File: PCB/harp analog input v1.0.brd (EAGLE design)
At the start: 86.8 x 80 mm, 112 parts, among them IC1 USBLC6-2SC6, IC10 SN74LVC1G125, IC11 SN74LVC1G125, IC12 SN74LVC1G125, IC13 AD7606-4, IC14 M74VHC1GT50DTT1G, IC15 M74VHC1GT50DTT1G, IC2 DC-DC-SIP-5, IC3 FT232RL, IC4 TPS78630DCQ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

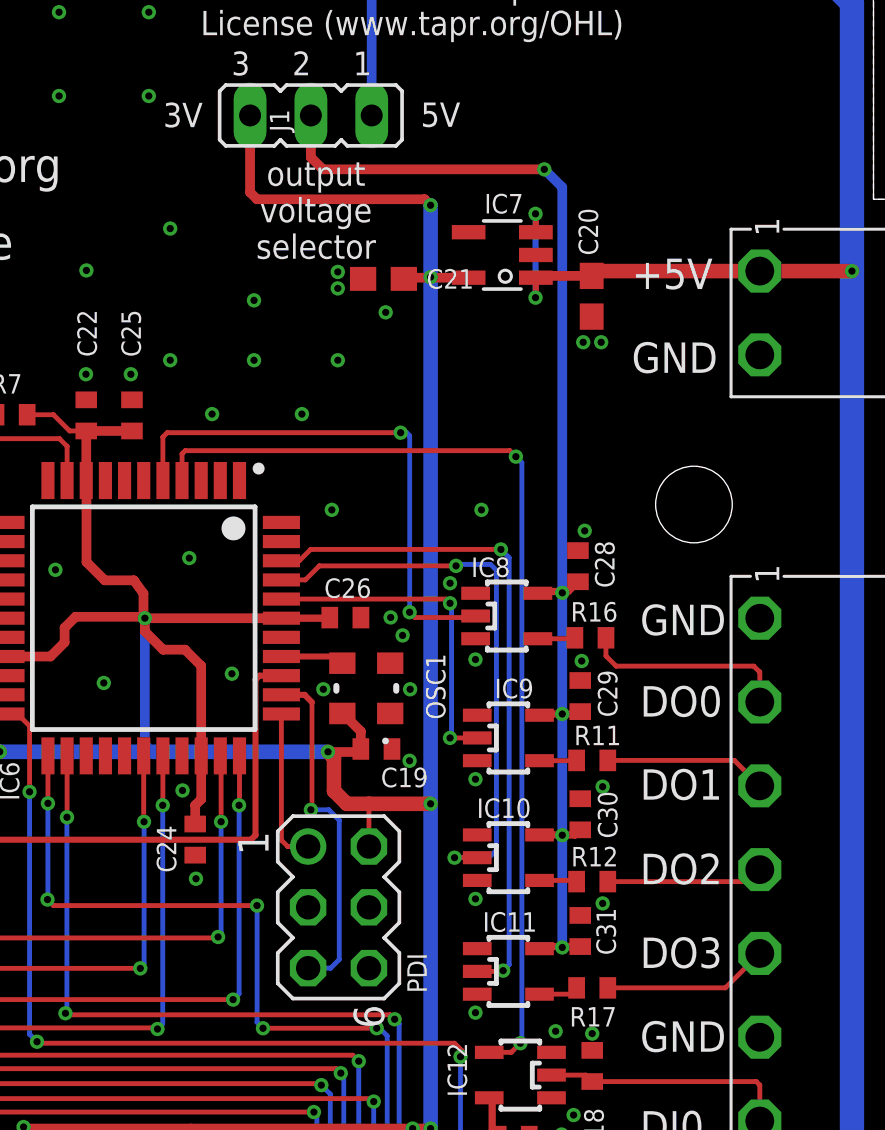
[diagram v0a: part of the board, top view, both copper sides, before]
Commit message: Re-organized DO alignment from left (DO0) to right (DO3)
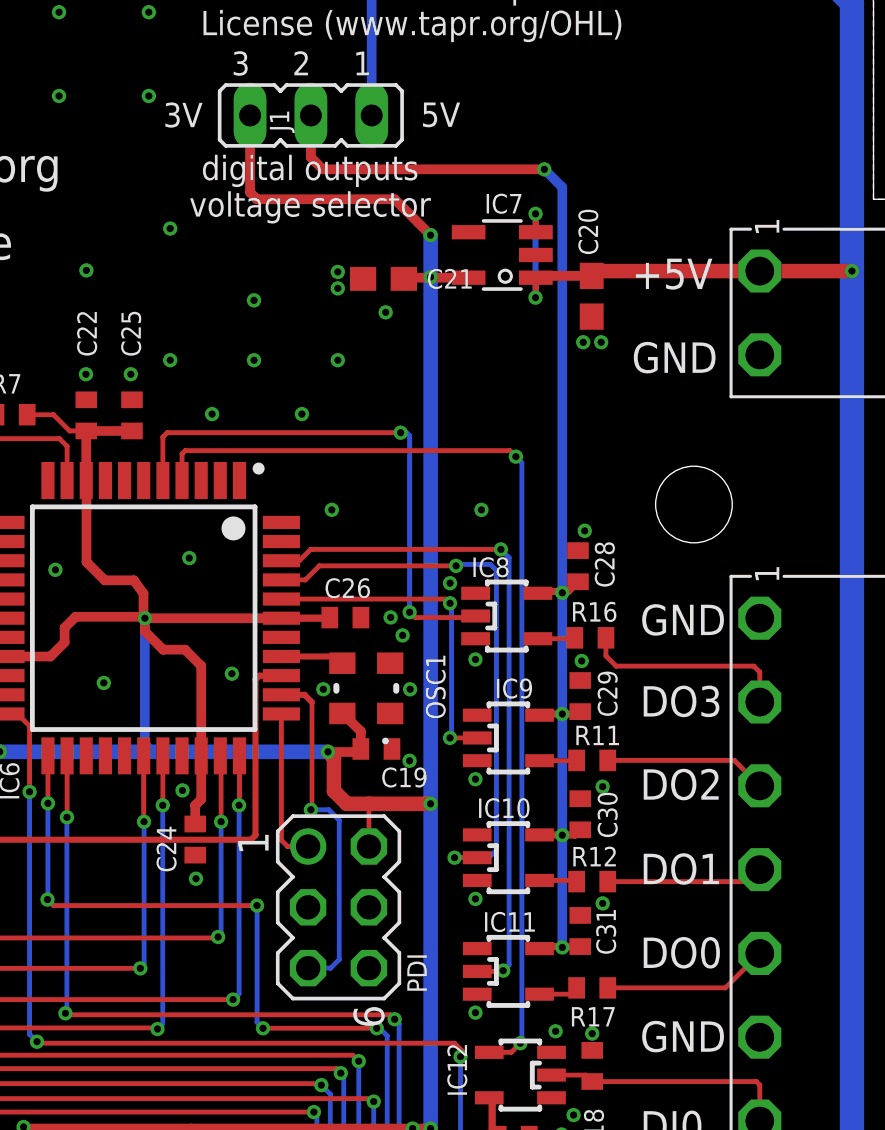
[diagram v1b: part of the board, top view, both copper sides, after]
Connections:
- net OUT00: now also IC11.2, IC6.42; no longer IC6.5, IC8.2
- net OUT01: now also IC10.2, IC6.41; no longer IC6.40, IC9.2
- net OUT02: now also IC6.40, IC9.2; no longer IC10.2, IC6.41
- net OUT03: now also IC6.5, IC8.2; no longer IC11.2, IC6.42
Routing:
- net OUT02: track 23.9 -> 14.0 mm
- net OUT01: track 14.0 -> 23.9 mm
- net OUT03: track 28.3 -> 22.5 mm
- net OUT00: track 22.5 -> 28.3 mm
- net VCCIO: track 259.3 -> 258.6 mm
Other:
- board text added: "digital outputs voltage selector"
- board text removed: "output voltage selector"
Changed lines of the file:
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@@
 <?xml version="1.0" encoding="utf-8"?>
 <!DOCTYPE eagle SYSTEM "eagle.dtd">
-<eagle version="9.6.2">
+<eagle version="9.5.1">
 <drawing>
 <settings>
@@
 <wire x1="77.763934375" y1="0" x2="80" y2="2.236065625" width="0" layer="20" curve="90"/>
 <wire x1="80" y1="2.236065625" x2="80" y2="24.75" width="0" layer="20"/>
-<text x="56.71518125" y="69.296703125" size="1.016" layer="21" font="vector" ratio="12" rot="SR0" align="center">output
-voltage
-selector</text>
+<text x="56.46518125" y="70.296703125" size="1.016" layer="21" font="vector" ratio="12" rot="SR0" align="center">digital outputs
+voltage selector</text>
 <text x="61.08744375" y="72.774265625" size="1.016" layer="21" font="vector" ratio="15" rot="SR0">5V</text>
 <text x="50.327321875" y="72.76088125" size="1.016" layer="21" font="vector" ratio="15" rot="SR0">3V</text>
 <wire x1="27" y1="66" x2="30.5" y2="66" width="0.2032" layer="41"/>
 <text x="70.25" y="51.545621875" size="1.27" layer="21" font="vector" ratio="15" rot="SR0">GND</text>
-<text x="70.25" y="41.1429" size="1.27" layer="21" font="vector" ratio="15" rot="SR0">DO2</text>
-<text x="70.25" y="37.6429" size="1.27" layer="21" font="vector" ratio="15" rot="SR0">DO3</text>
+<text x="70.25" y="41.1429" size="1.27" layer="21" font="vector" ratio="15" rot="SR0">DO1</text>
+<text x="70.25" y="37.6429" size="1.27" layer="21" font="vector" ratio="15" rot="SR0">DO0</text>
 <text x="70.25" y="34.1429" size="1.27" layer="21" font="vector" ratio="15" rot="SR0">GND</text>
 <text x="70.25" y="30.3929" size="1.27" layer="21" font="vector" ratio="15" rot="SR0">DI0</text>
-<text x="70.25" y="48.1429" size="1.27" layer="21" font="vector" ratio="15" rot="SR0">DO0</text>
-<text x="70.25" y="44.670621875" size="1.27" layer="21" font="vector" ratio="15" rot="SR0">DO1</text>
+<text x="70.25" y="48.1429" size="1.27" layer="21" font="vector" ratio="15" rot="SR0">DO3</text>
+<text x="70.25" y="44.670621875" size="1.27" layer="21" font="vector" ratio="15" rot="SR0">DO2</text>
 <text x="70.25" y="27.170621875" size="1.27" layer="21" font="vector" ratio="15" rot="SR0">GND</text>
 <text x="7.61" y="6.8098" size="1.524" layer="21" font="vector" ratio="15" rot="R90">IN_A0</text>
@@
 <wire x1="61.5" y1="30.9375" x2="61.83935625" y2="30.59814375" width="0.3048" layer="1"/>
 <via x="61.5" y="30.9375" extent="1-16" drill="0.3" diameter="0.6"/>
-<wire x1="61.5" y1="69.5" x2="61.5" y2="66.5" width="0.6096" layer="16"/>
+<wire x1="61.5" y1="68.25" x2="61.5" y2="66.5" width="0.6096" layer="16"/>
 <wire x1="61.5" y1="66.5" x2="61.5" y2="44.5" width="0.6096" layer="16"/>
 <wire x1="53.96" y1="73.25" x2="53.96" y2="70.04" width="0.4064" layer="1"/>
 <wire x1="53.96" y1="70.04" x2="54.25" y2="69.75" width="0.4064" layer="1"/>
-<wire x1="54.25" y1="69.75" x2="61.25" y2="69.75" width="0.4064" layer="1"/>
-<wire x1="61.5" y1="69.5" x2="61.25" y2="69.75" width="0.4064" layer="1"/>
-<via x="61.5" y="69.5" extent="1-16" drill="0.3" diameter="0.6"/>
+<wire x1="54.25" y1="69.75" x2="60" y2="69.75" width="0.4064" layer="1"/>
+<wire x1="61.5" y1="68.25" x2="60" y2="69.75" width="0.4064" layer="1"/>
+<via x="61.5" y="68.25" extent="1-16" drill="0.3" diameter="0.6"/>
 <wire x1="46.4271" y1="60.0729" x2="47.1181" y2="60.0729" width="0.2032" layer="1"/>
 <wire x1="44.65" y1="60.75" x2="45.75" y2="60.75" width="0.2032" layer="1"/>
@@
 <wire x1="65.3125" y1="58.75" x2="65.0625" y2="59" width="0.2032" layer="16"/>
 </signal>
-<signal name="OUT00">
+<signal name="OUT03">
 <contactref element="IC8" pad="2"/>
 <contactref element="IC6" pad="5"/>
@@
 <wire x1="67.3375" y1="36.55" x2="67.6" y2="36.8125" width="0.2032" layer="1"/>
 </signal>
-<signal name="OUT01">
+<signal name="OUT02">
 <contactref element="IC9" pad="2"/>
 <contactref element="IC6" pad="40"/>
@@
 <wire x1="62.1355" y1="53.052" x2="62.3125" y2="52.875" width="0.2032" layer="1"/>
 </signal>
-<signal name="OUT02">
+<signal name="OUT01">
 <contactref element="IC10" pad="2"/>
 <contactref element="IC6" pad="41"/>
@@
 <wire x1="62.5625" y1="54.4375" x2="62.625" y2="54.5" width="0.2032" layer="16"/>
 </signal>
-<signal name="OUT03">
+<signal name="OUT00">
 <contactref element="IC11" pad="2"/>
 <contactref element="IC6" pad="42"/>

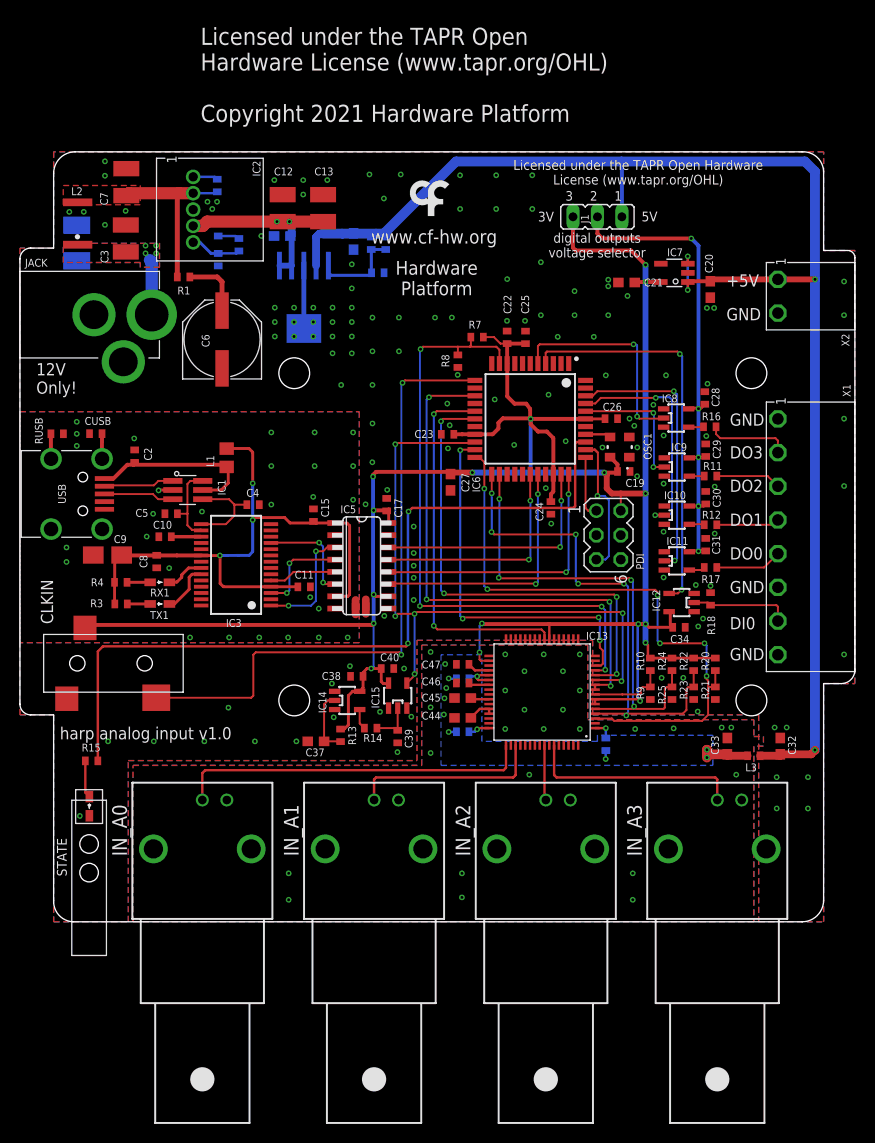
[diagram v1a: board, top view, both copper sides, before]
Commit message: Correct minor DRC and net labelling from merge
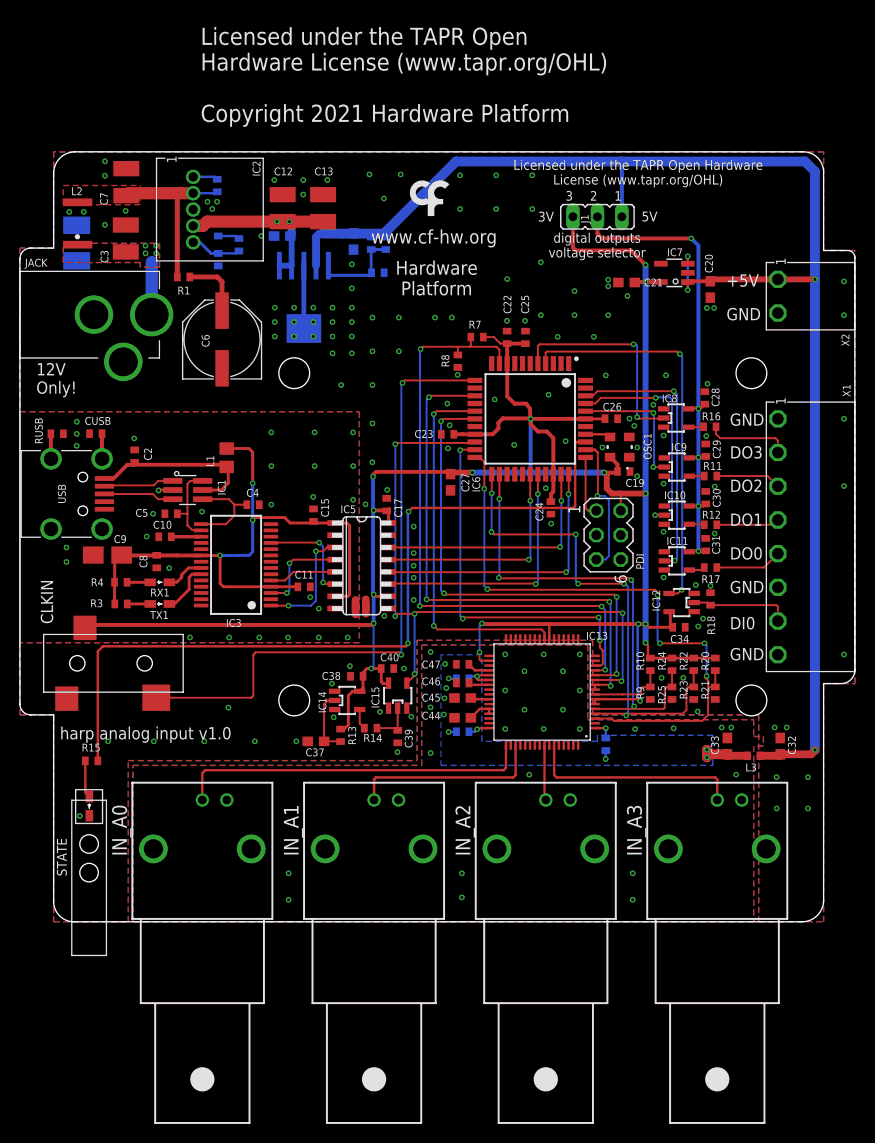
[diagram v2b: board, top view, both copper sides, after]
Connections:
- net OUT00 renamed OUT3
- net OUT01 renamed OUT2
- net OUT02 renamed OUT1
- net OUT03 renamed OUT0

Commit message: Add CONVST pin/swap CS_ADC
To allow for future higher speed acquisitions
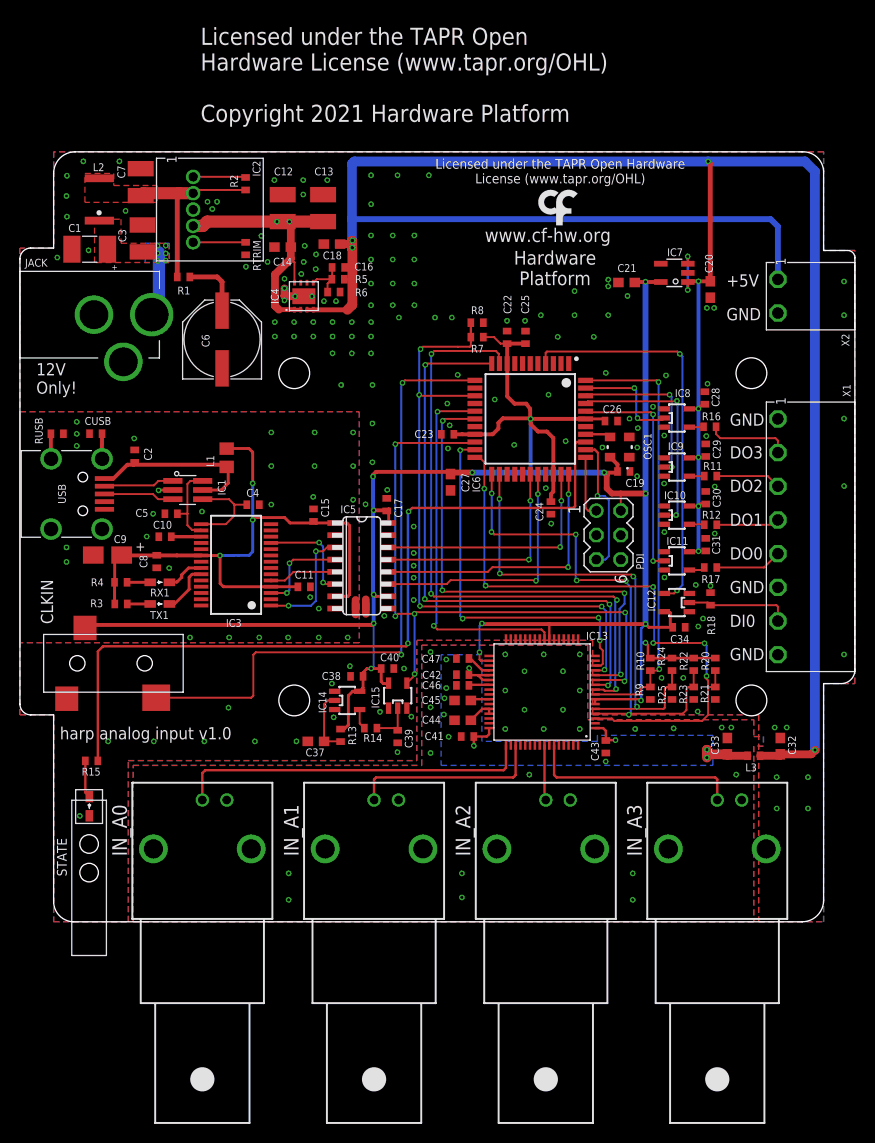
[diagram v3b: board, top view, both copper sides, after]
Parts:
- removed CTUNE: NA, rcl:C0402
- removed J1: (no value), jumper:JP2
- removed RTUNE: NA, rcl:R0402
- C37: value 10uF -> 10uF NA
- C38, C40: value 100nF -> 100nF NA
- C39: value 1uF -> 1uF NA
- IC4: device CNP:SOT223-6 -> CNP-ics 1:SON-8
- R10, R21, R22, R24: value 100k -> NA
- R13: value 20k -> 20k NA
- R14: value 40.2k -> 40.2k NA
- R7: value 3k -> 3k NA
- moved U$4 13.4 mm to (51.6, 74.8)
- moved R5 6.19 mm to (29.6, 66.8), flipped to the top, turned to 0 degrees
- moved R6 5.00 mm to (29.1, 65.4), flipped to the top, turned to 180 degrees
- moved R8 4.47 mm to (44.0, 62.2), turned to 180 degrees
- moved C16 4.24 mm to (29.6, 68.0), flipped to the top, turned to 180 degrees
- moved L2 3.36 mm to (4.75, 75.0)
- moved RTRIM 3.07 mm to (19.9, 69.9), flipped to the top
- moved R2 2.95 mm to (19.9, 76.7), flipped to the top
- moved C18 2.26 mm to (28.9, 70.4), flipped to the top, turned to 180 degrees
- moved C3 1.75 mm to (9.25, 71.0)
- moved C7 1.50 mm to (9.05, 76.8)
- moved C1 1.49 mm to (3.75, 69.9), flipped to the top, turned to 180 degrees
- moved C14 1.15 mm to (23.8, 70.1), flipped to the top, turned to 180 degrees
- moved C41 0.71 mm to (43.0, 19.2), flipped to the top, turned to 0 degrees
- moved C47 0.60 mm to (42.5, 27.3)
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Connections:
- removed net +V: C28.1, C29.1, C30.1, C31.1, IC10.5, IC11.5, IC8.5, IC9.5, J1.2
- removed net CONVST: IC13.10, IC13.9, IC6.14
- removed net N$1: IC13.8, R10.1, R9.2
- removed net N$14: CTUNE.1, RTUNE.1
- new net CONVSTA: IC13.9, IC6.10
- new net CONVSTB: IC13.10, IC6.11
- new net RANGE: IC13.8, IC6.44, R10.1, R9.2
- net !CS_ADC: now also IC6.14; no longer IC6.10
- net +5V: now also C28.1, C29.1, C30.1, C31.1, IC10.5, IC11.5, IC4.P3, IC4.P4, IC8.5, IC9.5; no longer IC4.P$4, J1.1
- net DO0: now also R17.2, X1.P5; no longer R16.2, X1.P2
- net DO1: now also R12.2, X1.P4; no longer R11.2, X1.P3
- net DO2: now also R11.2, X1.P3; no longer R12.2, X1.P4
- net DO3: now also R16.2, X1.P2; no longer R17.2, X1.P5
- net GND: now also IC4.P6, IC4.P9; no longer IC4.P$3, IC4.P$6
- net N$12: no longer CTUNE.2
- net N$20: now also IC4.P5; no longer IC4.P$5
- net OUT0: now also IC11.2, IC6.40; no longer IC6.5, IC8.2
- net OUT1: now also IC10.2, IC6.41; no longer IC6.40, IC9.2
- net OUT2: now also IC6.42, IC9.2; no longer IC10.2, IC6.41
- net OUT3: now also IC6.43, IC8.2; no longer IC11.2, IC6.42
- net P5.45V: now also IC4.P1, IC4.P2, IC4.P8; no longer IC4.P$1, IC4.P$2, RTUNE.2
- net VCCIO: no longer J1.3
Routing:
- net +5V: track 152.2 -> 246.6 mm, vias 4 -> 11
- net CONVSTA: track 0.00 -> 64.5 mm, vias 0 -> 4
- net CONVSTB: track 0.00 -> 60.8 mm, vias 0 -> 4
- net CONVST: track 56.0 -> 0.00 mm, vias 4 -> 0
- net +V: track 52.6 -> 0.00 mm, vias 5 -> 0
- net RANGE: track 0.00 -> 46.5 mm, vias 0 -> 2
- net OUT3: track 28.3 -> 11.3 mm
- net VCCIO: track 258.6 -> 244.5 mm, vias 17 -> 15
- net OUT1: track 14.0 -> 22.8 mm
- net N$1: track 8.03 -> 0.00 mm
- net OUT2: track 23.9 -> 17.2 mm
- net GND: track 10.5 -> 4.32 mm, vias 167 -> 180
- net P5.45V: track 25.7 -> 31.9 mm
- net N$20: track 9.40 -> 4.84 mm
- net !CS_ADC: track 65.2 -> 69.3 mm, vias 4 -> 5
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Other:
- board text added: "+"
- board text removed: "3V"
- board text removed: "5V"
- board text removed: "digital outputs voltage selector"
